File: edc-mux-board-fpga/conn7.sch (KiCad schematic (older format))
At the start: 24 parts

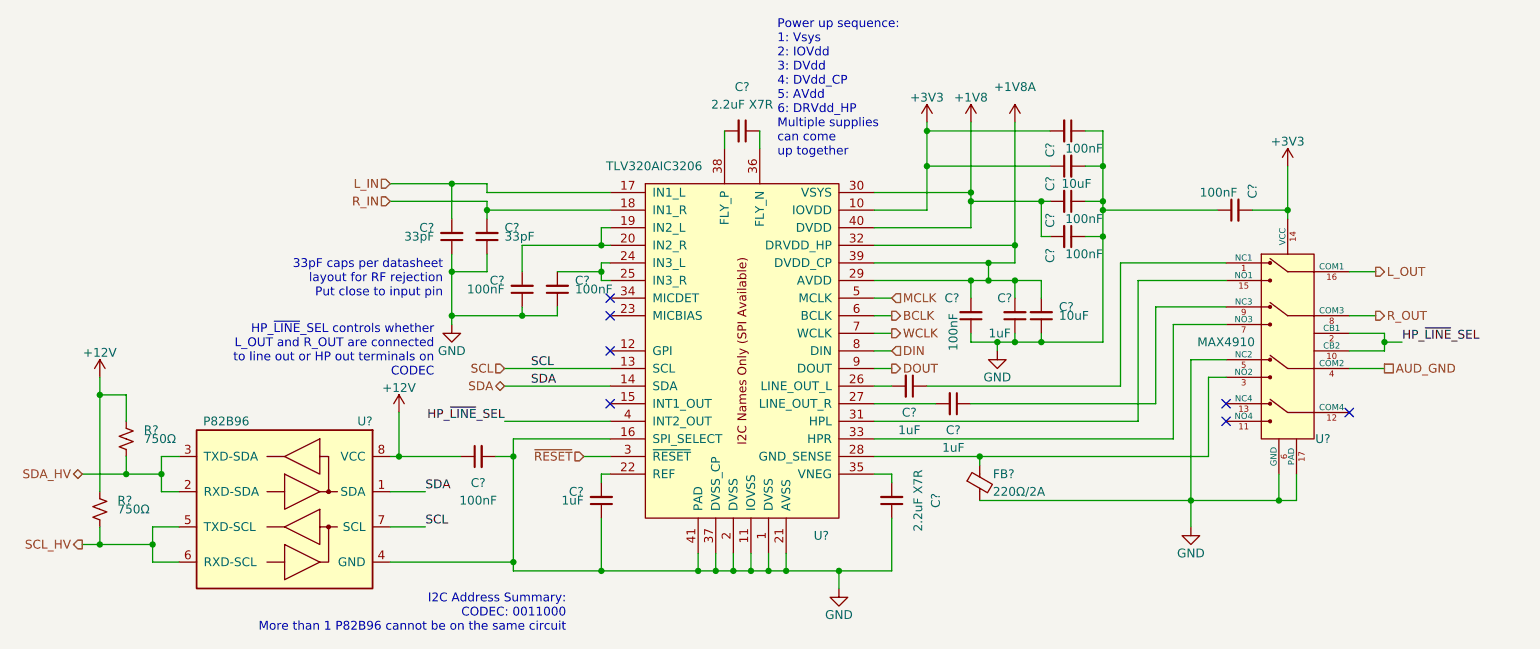
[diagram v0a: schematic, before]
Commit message: Finished FPGA and MCU interconnections.
Finished up interrupt wiring
Fixed a few missing connections
Annotated Schematic
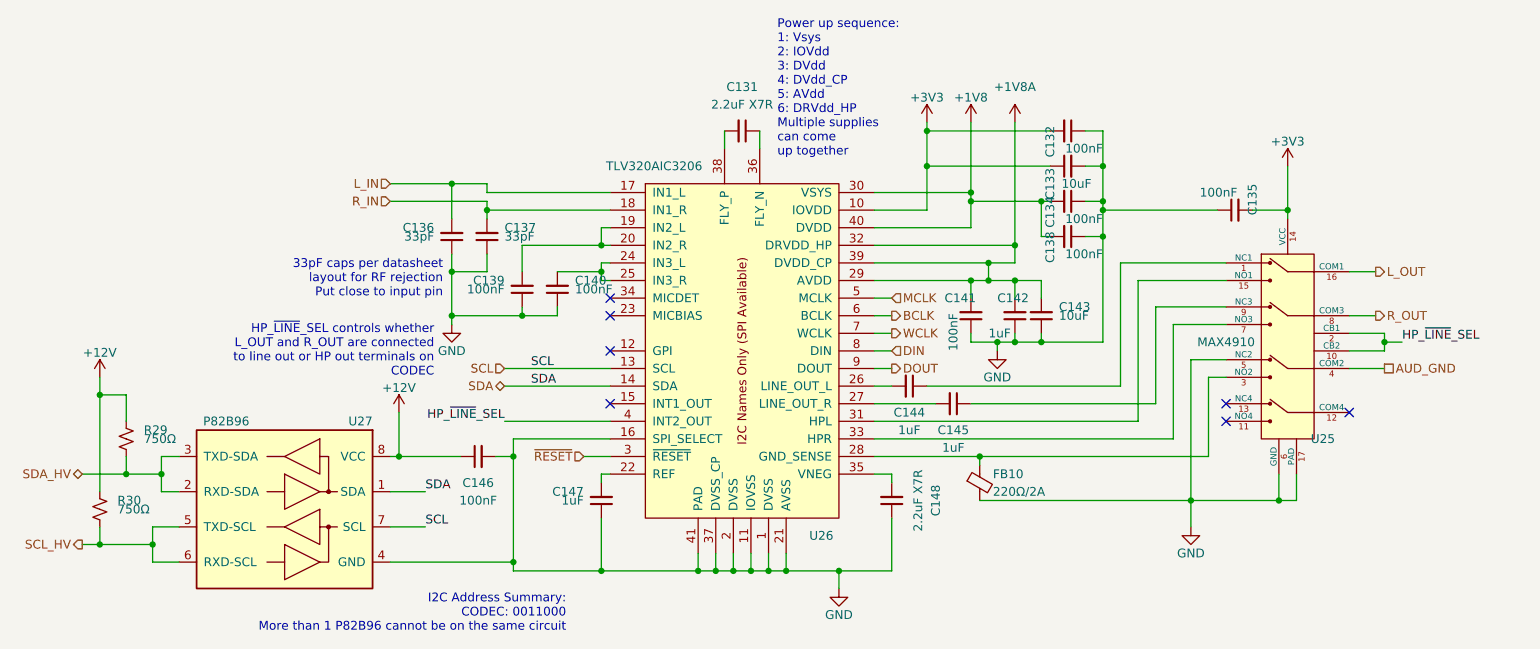
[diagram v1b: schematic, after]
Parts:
- removed C?: 1uF, Capacitor_SMD:C_0805_2012Metric, symbol Device:C_Small
- removed C? (x2): 2.2uF X7R, Capacitor_SMD:C_0603_1608Metric, symbol Device:C_Small
- removed C? (x2): 1uF, Capacitor_SMD:C_0603_1608Metric, symbol Device:C_Small
- removed C? (x6): 100nF, Capacitor_SMD:C_0603_1608Metric, symbol Device:C_Small
- removed C? (x2): 33pF, Capacitor_SMD:C_0603_1608Metric, symbol Device:C_Small
- removed C? (x2): 10uF, Capacitor_SMD:C_1206_3216Metric, symbol Device:C_Small
- removed FB?: 220Ω/2A, Resistor_SMD:R_0603_1608Metric, symbol Device:Ferrite_Bead_Small
- removed R?: 750Ω, Resistor_SMD:R_0603_1608Metric, symbol Device:R_Small_US
- removed U?: TLV320AIC3206, Package_DFN_QFN:UQFN-40-1EP_5x5mm_P0.4mm_EP3.8x3.8mm_ThermalVias, symbol SW-Texas:TLV320AIC3206
- removed U?: MAX4910, Package_DFN_QFN:TQFN-16-1EP_3x3mm_P0.5mm_EP1.23x1.23mm, symbol SW-dallas-semi-maxim:MAX4910
- removed U?: P82B96, Package_SO:TSSOP-8_3x3mm_P0.65mm, symbol Interface_Expansion:P82B96
- added C131, C148: 2.2uF X7R, Capacitor_SMD:C_0603_1608Metric, symbol Device:C_Small
- added C132, C135, C138, C139, C140, C141: 100nF, Capacitor_SMD:C_0603_1608Metric, symbol Device:C_Small
- added C133, C143: 10uF, Capacitor_SMD:C_1206_3216Metric, symbol Device:C_Small
- added C136, C137: 33pF, Capacitor_SMD:C_0603_1608Metric, symbol Device:C_Small
- added C142, C147: 1uF, Capacitor_SMD:C_0603_1608Metric, symbol Device:C_Small
- added C144: 1uF, Capacitor_SMD:C_0805_2012Metric, symbol Device:C_Small
- added FB10: 220Ω/2A, Resistor_SMD:R_0603_1608Metric, symbol Device:Ferrite_Bead_Small
- added R30: 750Ω, Resistor_SMD:R_0603_1608Metric, symbol Device:R_Small_US
- added U25: MAX4910, Package_DFN_QFN:TQFN-16-1EP_3x3mm_P0.5mm_EP1.23x1.23mm, symbol SW-dallas-semi-maxim:MAX4910
- added U26: TLV320AIC3206, Package_DFN_QFN:UQFN-40-1EP_5x5mm_P0.4mm_EP3.8x3.8mm_ThermalVias, symbol SW-Texas:TLV320AIC3206
- added U27: P82B96, Package_SO:TSSOP-8_3x3mm_P0.65mm, symbol Interface_Expansion:P82B96
- gave numbers to parts that had none: 4
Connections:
- net +12V: now also R30.1, U27.8 (VCC)
- net +1V8: now also C138.2, U26.30 (VSYS), U26.40 (DVDD)
- net +1V8A: now also C141.2, C142.2, C143.2, U26.29 (AVDD), U26.32 (DRVDD_HP), U26.39 (DVDD_CP)
- net +3V3: now also C132.2, C133.1, C135.2, U25.14 (VCC), U26.10 (IOVDD)
- net AUD_GND: now also U25.4 (COM2)
- net BCLK: now also U26.6 (BCLK)
- net DIN: now also U26.8 (DIN)
- net DOUT: now also U26.9 (DOUT)
- net GND: now also C132.1, C133.2, C135.1, C136.1, C137.1, C138.1, C139.1, C140.1, C141.1, C142.1, C143.1, C147.1, C148.1, FB10.2, U25.17 (PAD), U25.5 (NC2), U25.6 (GND), U26.1 (DVSS), U26.11 (IOVSS), U26.16 (SPI_SELECT), U26.2 (DVSS), U26.21 (AVSS), U26.37 (DVSS_CP), U26.41 (PAD), U27.4 (GND)
- net HP_~LINE~_SEL: now also U25.10 (CB2), U25.2 (CB1), U26.4 (INT2_OUT)
- net L_IN: now also C136.2, U26.17 (IN1_L)
- net L_OUT: now also U25.16 (COM1)
- net MCLK: now also U26.5 (MCLK)
- net R_IN: now also C137.2, U26.18 (IN1_R)
- net R_OUT: now also U25.8 (COM3)
- net SCL: now also U26.13 (SCL), U27.7 (SCL)
- net SCL_HV: now also R30.2, U27.5 (TXD-SCL), U27.6 (RXD-SCL)
- net SDA: now also U26.14 (SDA), U27.1 (SDA)
- net SDA_HV: now also U27.2 (RXD-SDA), U27.3 (TXD-SDA)
- net WCLK: now also U26.7 (WCLK)
- net ~RESET: now also U26.3 (~RESET)
- net at C145.1: now also U25.9 (NC3)
- net at C145.2: now also U26.27 (LINE_OUT_R)
- new net: C144.1, U25.1 (NC1)
- new net: C144.2, U26.26 (LINE_OUT_L)
- new net: C139.2, U26.19 (IN2_L), U26.20 (IN2_R)
- new net: C147.2, U26.22 (REF)
- new net: C140.2, U26.24 (IN3_L), U26.25 (IN3_R)
- new net: FB10.1, U25.3 (NO2), U26.28 (GND_SENSE)
- new net: U25.15 (NO1), U26.31 (HPL)
- new net: U25.7 (NO3), U26.33 (HPR)
- new net: C148.2, U26.35 (VNEG)
- new net: C131.1, U26.36 (FLY_N)
- new net: C131.2, U26.38 (FLY_P)
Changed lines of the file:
@@
 $EndDescr
 $Comp
-L SW-Texas:TLV320AIC3206 U?
-U 1 1 5CE6F2E7
+L SW-Texas:TLV320AIC3206 U26
+U 1 1 5DAC04B9
 P 5200 3400
-F 0 "U?" H 5650 2350 50  0000 C CNN
+F 0 "U26" H 5650 2350 50  0000 C CNN
 F 1 "TLV320AIC3206" H 4700 4450 50  0000 C CNN
 F 2 "Package_DFN_QFN:UQFN-40-1EP_5x5mm_P0.4mm_EP3.8x3.8mm_ThermalVias" H 5250 4800 50  0001 C CNN
@@
 $EndComp
 $Comp
-L Device:C_Small C?
-U 1 1 5CE6F309
+L Device:C_Small C131
+U 1 1 5DAC04C1
 P 5200 2150
-F 0 "C?" V 4950 2150 50  0000 C CNN
+F 0 "C131" V 4950 2150 50  0000 C CNN
 F 1 "2.2uF X7R" V 5050 2150 50  0000 C CNN
 F 2 "Capacitor_SMD:C_0603_1608Metric" H 5200 2150 50  0001 C CNN
@@
 	5300 2250 5300 2150
 $Comp
-L Device:C_Small C?
-U 1 1 5CE6F311
+L Device:C_Small C148
+U 1 1 5DAC04D7
 P 6050 4250
-F 0 "C?" V 5800 4250 50  0000 C CNN
+F 0 "C148" V 5800 4250 50  0000 C CNN
 F 1 "2.2uF X7R" V 5900 4250 50  0000 C CNN
 F 2 "Capacitor_SMD:C_0603_1608Metric" H 6050 4250 50  0001 C CNN
@@
 	6050 4100 6050 4150
 $Comp
-L power:GND #PWR?
-U 1 1 5CE6F323
+L power:GND #PWR091
+U 1 1 5DAC04DF
 P 5750 4750
-F 0 "#PWR?" H 5750 4500 50  0001 C CNN
+F 0 "#PWR091" H 5750 4500 50  0001 C CNN
 F 1 "GND" H 5750 4600 50  0000 C CNN
 F 2 "" H 5750 4750 50  0001 C CNN
@@
 	5450 4650 5750 4650
 $Comp
-L Device:C_Small C?
-U 1 1 5CE6F329
+L Device:C_Small C147
+U 1 1 5DAC04EE
 P 4400 4250
-F 0 "C?" H 4500 4200 50  0000 L CNN
+F 0 "C147" H 4500 4200 50  0000 L CNN
 F 1 "1uF" H 4500 4250 50  0000 L CNN
 F 2 "Capacitor_SMD:C_0603_1608Metric" H 4400 4250 50  0001 C CNN
@@
 Connection ~ 4950 4650
 $Comp
-L Device:C_Small C?
-U 1 1 5CE6F348
+L Device:C_Small C139
+U 1 1 5DAC04FC
 P 3950 3050
-F 0 "C?" H 4050 3000 50  0000 L CNN
+F 0 "C139" H 4050 3000 50  0000 L CNN
 F 1 "100nF" H 4050 3050 50  0000 L CNN
 F 2 "Capacitor_SMD:C_0603_1608Metric" H 3950 3050 50  0001 C CNN
@@
 $EndComp
 $Comp
-L Device:C_Small C?
-U 1 1 5CE6F363
+L Device:C_Small C140
+U 1 1 5DAC0512
 P 4150 3050
-F 0 "C?" H 4050 3000 50  0000 R CNN
+F 0 "C140" H 4050 3000 50  0000 R CNN
 F 1 "100nF" H 4050 3050 50  0000 R CNN
 F 2 "Capacitor_SMD:C_0603_1608Metric" H 4150 3050 50  0001 C CNN
@@
 Connection ~ 4400 2950
 $Comp
-L power:GND #PWR?
-U 1 1 5CE6F368
+L power:GND #PWR086
+U 1 1 5DAC0518
 P 3550 3250
-F 0 "#PWR?" H 3550 3000 50  0001 C CNN
+F 0 "#PWR086" H 3550 3000 50  0001 C CNN
 F 1 "GND" H 3550 3100 50  0000 C CNN
 F 2 "" H 3550 3250 50  0001 C CNN
@@
 	8650 3300 8850 3300
 $Comp
-L SW-dallas-semi-maxim:MAX4910 U?
-U 1 1 5CE6F375
+L SW-dallas-semi-maxim:MAX4910 U25
+U 1 1 5DAC0527
 P 8300 3350
-F 0 "U?" H 8500 2800 50  0000 C CNN
+F 0 "U25" H 8500 2800 50  0000 C CNN
 F 1 "MAX4910" H 7950 3350 50  0000 C CNN
 F 2 "Package_DFN_QFN:TQFN-16-1EP_3x3mm_P0.5mm_EP1.23x1.23mm" H 9950 4500 50  0001 C CNN
@@
 	7750 3450 7750 4250
 $Comp
-L power:GND #PWR?
+L power:GND #PWR090
 U 1 1 5CE6F387
 P 7750 4400
-F 0 "#PWR?" H 7750 4150 50  0001 C CNN
+F 0 "#PWR090" H 7750 4150 50  0001 C CNN
 F 1 "GND" H 7750 4250 50  0000 C CNN
 F 2 "" H 7750 4400 50  0001 C CNN
@@
 	8650 3500 8850 3500
 $Comp
-L Device:Ferrite_Bead_Small FB?
-U 1 1 5CE6F39A
+L Device:Ferrite_Bead_Small FB10
+U 1 1 5DAC0548
 P 6550 4150
-F 0 "FB?" H 6625 4200 50  0000 L CNN
+F 0 "FB10" H 6625 4200 50  0000 L CNN
 F 1 "220Ω/2A" H 6625 4100 50  0000 L CNN
 F 2 "Resistor_SMD:R_0603_1608Metric" V 6480 4150 50  0001 C CNN
@@
 	3750 2600 4450 2600
 $Comp
-L Device:C_Small C?
-U 1 1 5CE6F3AC
+L Device:C_Small C136
+U 1 1 5DAC055D
 P 3550 2750
-F 0 "C?" H 3650 2700 50  0000 L CNN
+F 0 "C136" H 3650 2700 50  0000 L CNN
 F 1 "33pF" H 3650 2750 50  0000 L CNN
 F 2 "Capacitor_SMD:C_0603_1608Metric" H 3550 2750 50  0001 C CNN
@@
 	3200 2550 3750 2550
 $Comp
-L Device:C_Small C?
-U 1 1 5CE6F3B7
+L Device:C_Small C137
+U 1 1 5DAC0562
 P 3750 2750
-F 0 "C?" H 3650 2700 50  0000 R CNN
+F 0 "C137" H 3650 2700 50  0000 R CNN
 F 1 "33pF" H 3650 2750 50  0000 R CNN
 F 2 "Capacitor_SMD:C_0603_1608Metric" H 3750 2750 50  0001 C CNN
@@
 	5950 3000 6500 3000
 $Comp
-L SW-power:+1V8A #+1V8A?
-U 1 1 5CE6F3C8
+L SW-power:+1V8A #+1V8A09
+U 1 1 5DAC0575
 P 6750 2100
-F 0 "#+1V8A?" H 7500 1800 60  0001 C CNN
+F 0 "#+1V8A09" H 7500 1800 60  0001 C CNN
 F 1 "+1V8A" H 6750 2300 50  0000 C CNN
 F 2 "" H 6750 2100 60  0001 C CNN
@@
 $EndComp
 $Comp
-L power:+1V8 #PWR?
-U 1 1 5CE6F3D1
+L power:+1V8 #PWR084
+U 1 1 5DAC058B
 P 6500 2100
-F 0 "#PWR?" H 6500 1950 50  0001 C CNN
+F 0 "#PWR084" H 6500 1950 50  0001 C CNN
 F 1 "+1V8" H 6500 2240 50  0000 C CNN
 F 2 "" H 6500 2100 50  0001 C CNN
@@
 	6750 2800 6750 2900
 $Comp
-L power:+3V3 #PWR?
-U 1 1 5CE6F3E5
+L power:+3V3 #PWR083
+U 1 1 5DAC058E
 P 6250 2100
-F 0 "#PWR?" H 6250 1950 50  0001 C CNN
+F 0 "#PWR083" H 6250 1950 50  0001 C CNN
 F 1 "+3V3" H 6250 2240 50  0000 C CNN
 F 2 "" H 6250 2100 50  0001 C CNN
@@
 	6250 2600 6250 2350
 $Comp
-L Device:C_Small C?
-U 1 1 5CE6F3F4
+L Device:C_Small C142
+U 1 1 5DAC05AA
 P 6750 3200
-F 0 "C?" H 6850 3100 50  0000 R CNN
+F 0 "C142" H 6850 3100 50  0000 R CNN
 F 1 "1uF" H 6900 3300 50  0000 R CNN
 F 2 "Capacitor_SMD:C_0603_1608Metric" H 6750 3200 50  0001 C CNN
@@
 $EndComp
 $Comp
-L power:GND #PWR?
-U 1 1 5CE6F403
+L power:GND #PWR087
+U 1 1 5DAC05B1
 P 6650 3400
-F 0 "#PWR?" H 6650 3150 50  0001 C CNN
+F 0 "#PWR087" H 6650 3150 50  0001 C CNN
 F 1 "GND" H 6650 3250 50  0000 C CNN
 F 2 "" H 6650 3400 50  0001 C CNN
@@
 $EndComp
 $Comp
-L Device:C_Small C?
-U 1 1 5CE6F40F
+L Device:C_Small C143
+U 1 1 5DAC05C9
 P 6900 3200
-F 0 "C?" H 6800 3150 50  0000 R CNN
+F 0 "C143" H 6800 3150 50  0000 R CNN
 F 1 "10uF" H 6800 3200 50  0000 R CNN
 F 2 "Capacitor_SMD:C_1206_3216Metric" H 6900 3200 50  0001 C CNN
@@
 $EndComp
 $Comp
-L Device:C_Small C?
-U 1 1 5CE6F425
+L Device:C_Small C141
+U 1 1 5DAC05CB
 P 6500 3200
-F 0 "C?" H 6650 3100 50  0000 R CNN
+F 0 "C141" H 6650 3100 50  0000 R CNN
 F 1 "100nF" V 6600 3400 50  0000 R CNN
 F 2 "Capacitor_SMD:C_0603_1608Metric" H 6500 3200 50  0001 C CNN
@@
 	6650 3350 6750 3350
 $Comp
-L Device:C_Small C?
-U 1 1 5CE6F42F
+L Device:C_Small C132
+U 1 1 5DAC05DA
 P 7050 2150
-F 0 "C?" H 7200 2050 50  0000 R CNN
+F 0 "C132" H 7200 2050 50  0000 R CNN
 F 1 "100nF" V 7150 2350 50  0000 R CNN
 F 2 "Capacitor_SMD:C_0603_1608Metric" H 7050 2150 50  0001 C CNN
@@
 $EndComp
 $Comp
-L Device:C_Small C?
-U 1 1 5CE6F439
+L Device:C_Small C133
+U 1 1 5DAC05F0
 P 7050 2350
-F 0 "C?" H 6950 2450 50  0000 C CNN
+F 0 "C133" H 6950 2450 50  0000 C CNN
 F 1 "10uF" V 6950 2300 50  0000 C CNN
 F 2 "Capacitor_SMD:C_1206_3216Metric" H 7050 2350 50  0001 C CNN
@@
 	6250 2150 6250 2100
 $Comp
-L Device:C_Small C?
+L Device:C_Small C134
 U 1 1 5CE6F451
 P 7050 2550
-F 0 "C?" H 7200 2450 50  0000 R CNN
+F 0 "C134" H 7200 2450 50  0000 R CNN
 F 1 "100nF" V 7150 2750 50  0000 R CNN
 F 2 "Capacitor_SMD:C_0603_1608Metric" H 7050 2550 50  0001 C CNN
@@
 	6500 2550 6500 2500
 $Comp
-L Device:C_Small C?
-U 1 1 5CE6F456
+L Device:C_Small C138
+U 1 1 5DAC0611
 P 7050 2750
-F 0 "C?" H 7200 2650 50  0000 R CNN
+F 0 "C138" H 7200 2650 50  0000 R CNN
 F 1 "100nF" V 7150 2950 50  0000 R CNN
 F 2 "Capacitor_SMD:C_0603_1608Metric" H 7050 2750 50  0001 C CNN
@@
 NoConn ~ 8650 3750
 $Comp
-L Device:C_Small C?
-U 1 1 5CE6F46F
+L Device:C_Small C135
+U 1 1 5DAC061A
 P 8000 2600
-F 0 "C?" H 8150 2500 50  0000 R CNN
+F 0 "C135" H 8150 2500 50  0000 R CNN
 F 1 "100nF" V 8100 2800 50  0000 R CNN
 F 2 "Capacitor_SMD:C_0603_1608Metric" H 8000 2600 50  0001 C CNN
@@
 $EndComp
 $Comp
-L power:+3V3 #PWR?
-U 1 1 5CE6F47E
+L power:+3V3 #PWR085
+U 1 1 5DAC062F
 P 8300 2350
-F 0 "#PWR?" H 8300 2200 50  0001 C CNN
+F 0 "#PWR085" H 8300 2200 50  0001 C CNN
 F 1 "+3V3" H 8300 2490 50  0000 C CNN
 F 2 "" H 8300 2350 50  0001 C CNN
@@
 	8250 4250 8350 4250
 $Comp
-L Interface_Expansion:P82B96 U?
-U 1 1 5CE6F489
+L Interface_Expansion:P82B96 U27
+U 1 1 5DAC063B
 P 2600 4300
-F 0 "U?" H 2100 4800 50  0000 L CNN
+F 0 "U27" H 2100 4800 50  0000 L CNN
 F 1 "P82B96" H 2800 4800 50  0000 L CNN
 F 2 "Package_SO:TSSOP-8_3x3mm_P0.65mm" H 2600 4300 50  0001 C CNN
@@
 $EndComp
 $Comp
-L power:+12V #PWR?
-U 1 1 5CE6F490
+L power:+12V #PWR088
+U 1 1 5DAC0645
 P 1550 3550
-F 0 "#PWR?" H 1550 3400 50  0001 C CNN
+F 0 "#PWR088" H 1550 3400 50  0001 C CNN
 F 1 "+12V" H 1550 3690 50  0000 C CNN
 F 2 "" H 1550 3550 50  0001 C CNN
@@
 	1900 4100 1900 4200
 $Comp
-L Device:R_Small_US R?
+L Device:R_Small_US R29
 U 1 1 5CE6F4C1
 P 1700 3900
-F 0 "R?" H 1800 3950 50  0000 L CNN
+F 0 "R29" H 1800 3950 50  0000 L CNN
 F 1 "750Ω" H 1800 3900 50  0000 L CNN
 F 2 "Resistor_SMD:R_0603_1608Metric" H 1700 3900 50  0001 C CNN
@@
 $EndComp
 $Comp
-L Device:R_Small_US R?
-U 1 1 5CE6F4D0
+L Device:R_Small_US R30
+U 1 1 5DAC066C
 P 1550 4300
-F 0 "R?" H 1650 4350 50  0000 L CNN
+F 0 "R30" H 1650 4350 50  0000 L CNN
 F 1 "750Ω" H 1650 4300 50  0000 L CNN
 F 2 "Resistor_SMD:R_0603_1608Metric" H 1550 4300 50  0001 C CNN
@@
 	1700 4100 1900 4100
 $Comp
-L power:+12V #PWR?
-U 1 1 5CE6F4E1
+L power:+12V #PWR089
+U 1 1 5DAC0670
 P 3250 3750
-F 0 "#PWR?" H 3250 3600 50  0001 C CNN
+F 0 "#PWR089" H 3250 3600 50  0001 C CNN
 F 1 "+12V" H 3250 3890 50  0000 C CNN
 F 2 "" H 3250 3750 50  0001 C CNN
@@
 	3200 4400 3400 4400
 $Comp
-L Device:C_Small C?
+L Device:C_Small C146
 U 1 1 5CE6F4F3
 P 3700 4000
-F 0 "C?" V 3550 4000 50  0000 C CNN
+F 0 "C146" V 3550 4000 50  0000 C CNN
 F 1 "100nF" V 3450 4000 50  0000 C CNN
 F 2 "Capacitor_SMD:C_0603_1608Metric" H 3700 4000 50  0001 C CNN
@@
 	1450 4500 1550 4500
 $Comp
-L Device:C_Small C?
-U 1 1 5CE6F2C0
+L Device:C_Small C144
+U 1 1 5DAC0498
 P 6150 3600
-F 0 "C?" V 6300 3600 50  0000 C CNN
+F 0 "C144" V 6300 3600 50  0000 C CNN
 F 1 "1uF" V 6400 3600 50  0000 C CNN
 F 2 "Capacitor_SMD:C_0805_2012Metric" H 6150 3600 50  0001 C CNN
@@
 $EndComp
 $Comp
-L Device:C_Small C?
+L Device:C_Small C145
 U 1 1 5CE6F2D4
 P 6400 3700
-F 0 "C?" V 6550 3700 50  0000 C CNN
+F 0 "C145" V 6550 3700 50  0000 C CNN
 F 1 "1uF" V 6650 3700 50  0000 C CNN
 F 2 "Capacitor_SMD:C_0805_2012Metric" H 6400 3700 50  0001 C CNN

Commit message: assigned more footprints
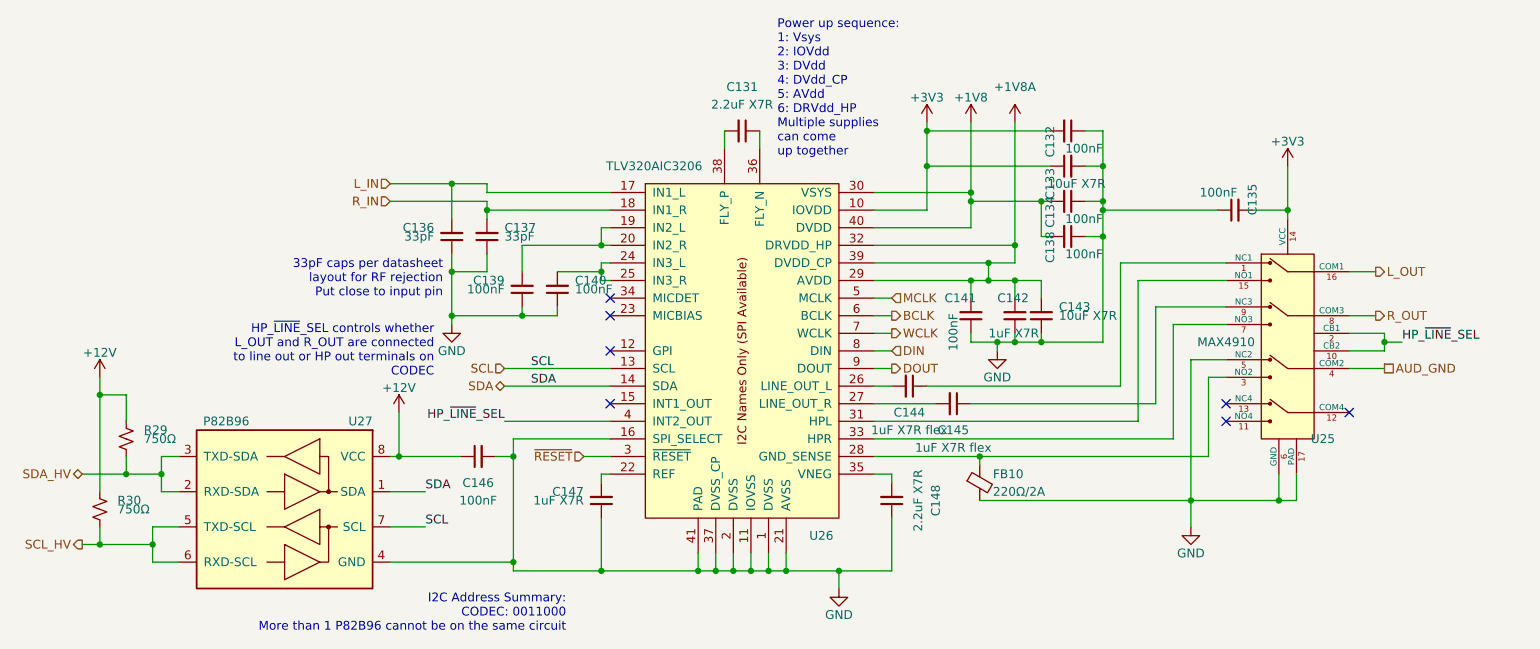
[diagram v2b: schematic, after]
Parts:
- C133, C143: value 10uF -> 10uF X7R
- C142, C147: value 1uF -> 1uF X7R
- C144, C145: value 1uF -> 1uF X7R flex
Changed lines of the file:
@@
 P 4400 4250
 F 0 "C147" H 4500 4200 50  0000 L CNN
-F 1 "1uF" H 4500 4250 50  0000 L CNN
+F 1 "1uF X7R" H 4500 4250 50  0000 L CNN
 F 2 "Capacitor_SMD:C_0603_1608Metric" H 4400 4250 50  0001 C CNN
 F 3 "~" H 4400 4250 50  0001 C CNN
@@
 P 6750 3200
 F 0 "C142" H 6850 3100 50  0000 R CNN
-F 1 "1uF" H 6900 3300 50  0000 R CNN
+F 1 "1uF X7R" H 6900 3300 50  0000 R CNN
 F 2 "Capacitor_SMD:C_0603_1608Metric" H 6750 3200 50  0001 C CNN
 F 3 "~" H 6750 3200 50  0001 C CNN
@@
 P 6900 3200
 F 0 "C143" H 6800 3150 50  0000 R CNN
-F 1 "10uF" H 6800 3200 50  0000 R CNN
+F 1 "10uF X7R" H 6800 3200 50  0000 R CNN
 F 2 "Capacitor_SMD:C_1206_3216Metric" H 6900 3200 50  0001 C CNN
 F 3 "~" H 6900 3200 50  0001 C CNN
@@
 P 7050 2350
 F 0 "C133" H 6950 2450 50  0000 C CNN
-F 1 "10uF" V 6950 2300 50  0000 C CNN
+F 1 "10uF X7R" V 6950 2300 50  0000 C CNN
 F 2 "Capacitor_SMD:C_1206_3216Metric" H 7050 2350 50  0001 C CNN
 F 3 "~" H 7050 2350 50  0001 C CNN
@@
 P 6150 3600
 F 0 "C144" V 6300 3600 50  0000 C CNN
-F 1 "1uF" V 6400 3600 50  0000 C CNN
+F 1 "1uF X7R flex" V 6400 3600 50  0000 C CNN
 F 2 "Capacitor_SMD:C_0805_2012Metric" H 6150 3600 50  0001 C CNN
 F 3 "~" H 6150 3600 50  0001 C CNN
@@
 P 6400 3700
 F 0 "C145" V 6550 3700 50  0000 C CNN
-F 1 "1uF" V 6650 3700 50  0000 C CNN
+F 1 "1uF X7R flex" V 6650 3700 50  0000 C CNN
 F 2 "Capacitor_SMD:C_0805_2012Metric" H 6400 3700 50  0001 C CNN
 F 3 "~" H 6400 3700 50  0001 C CNN
